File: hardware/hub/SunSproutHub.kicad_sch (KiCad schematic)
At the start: 48 parts, among them CN5 1755736, J4 BATTERY, J6 Qwiic Sys, J7 GPIO_HEADER_L, J8 GPIO_HEADER_R, Q1 MDD3415, Q2 DMP3098L-7, SW1 RESET, SW2 BOOT, U1 ESP32-C5-WROOM-1U

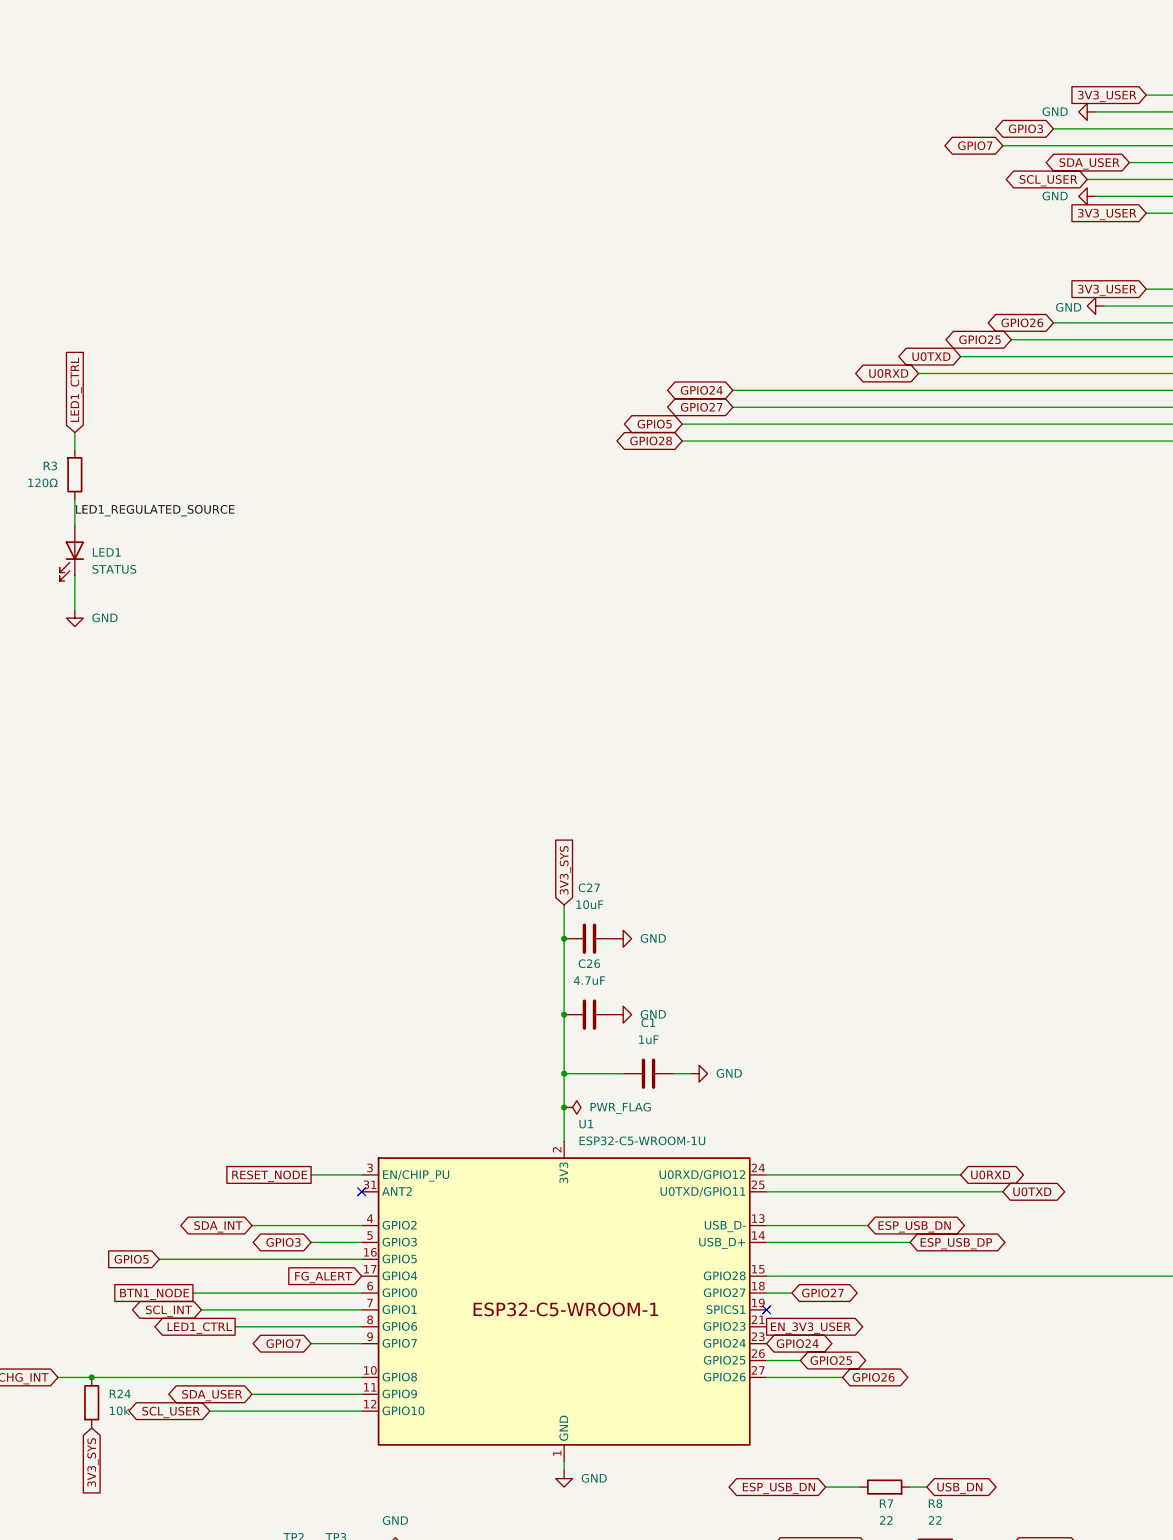
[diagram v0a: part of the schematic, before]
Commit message: Move the internal I2C clock to GPIO3 so both buses can run at once
The ESP32-C5 has one general-purpose I2C controller and one low-power
controller (datasheet 4.2.1.3: "ESP32-C5 has an I2C and an LP I2C bus
interface"). Running two I2C buses simultaneously needs both of them.

The general-purpose controller routes to any pin through the GPIO matrix. The
low-power one does not -- LP_I2C is wired through the LP IO MUX to GPIO2 for
data and GPIO3 for clock, and cannot be moved.

SDA_INT was already on GPIO2, but SCL_INT sat on GPIO1. That left neither bus
able to reach the low-power controller, so both contended for the single
general-purpose one and the firmware would not build. Caught while writing
example ESPHome firmware, before any board was fabricated.

SCL_INT now lands on GPIO3, which previously went only to the unfitted J7
expansion header. GPIO1 takes its place there as the spare, so no pin is lost.
The symbol pin names were updated to LP_I2C_SDA / LP_I2C_SCL to make the
constraint visible in the schematic.

This also gains something rather than just unblocking the build: LP peripherals
and the LP CPU stay powered in deep sleep, so the charger and fuel gauge on the
internal bus stay reachable while the main processor is off -- which suits a
node that sleeps ten minutes at a time.

Fixes a silkscreen mismatch found alongside it: J7 pin 3 read GPIO1 on the
front and GPIO3 on the back. All ten front/back label pairs now agree.

Verified with libraries present: DRC 0 violations, 0 unconnected, 0 schematic
parity; ERC matches the accepted baseline. Docs and board renders regenerated.

Co-Authored-By: Claude Opus 5 <noreply@anthropic.com>
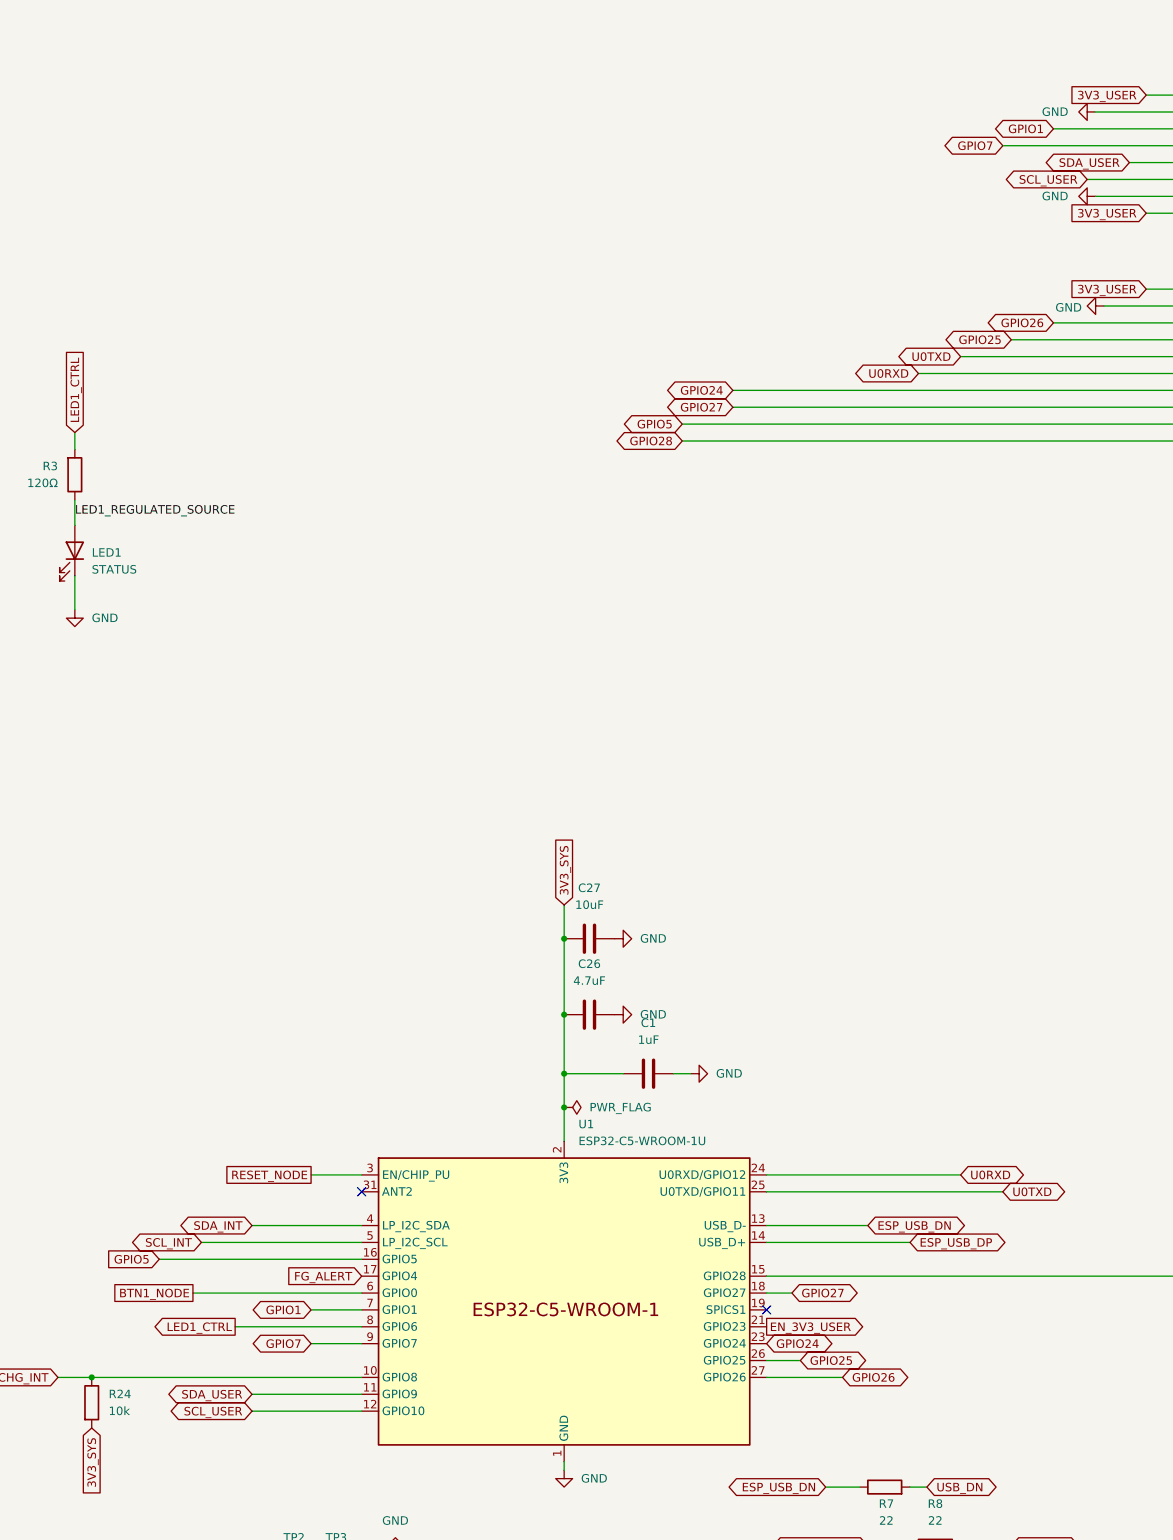
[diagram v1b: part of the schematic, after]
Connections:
- net SCL_INT: now also U1.5 (GPIO3); no longer U1.7 (GPIO1)
- net GPIO3 renamed GPIO1
- net GPIO1: now also U1.7 (GPIO1); no longer U1.5 (GPIO3)
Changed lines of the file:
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@@
 	(wire
 		(pts
+			(xy 405.13 227.33) (xy 381 227.33)
+		)
+		(stroke
+			(width 0)
+			(type default)
+		)
+	)
+	(wire
+		(pts
 			(xy 452.12 201.93) (xy 454.66 201.93)
 		)
@@
 	(wire
 		(pts
-			(xy 405.13 252.73) (xy 382.27 252.73)
+			(xy 405.13 252.73) (xy 388.62 252.73)
 		)
 		(stroke
@@
 	(wire
 		(pts
-			(xy 405.13 227.33) (xy 397.51 227.33)
-		)
-		(stroke
-			(width 0)
-			(type default)
-		)
-	)
-	(wire
-		(pts
 			(xy 474.98 264.16) (xy 480.06 264.16)
 		)
@@
 	(wire
 		(pts
-			(xy 405.13 237.49) (xy 381 237.49)
+			(xy 271.78 125.73) (xy 256.54 125.73)
 		)
 		(stroke
@@
 	(wire
 		(pts
-			(xy 271.78 125.73) (xy 256.54 125.73)
+			(xy 196.85 49.53) (xy 196.85 43.18)
 		)
 		(stroke
@@
 	(wire
 		(pts
-			(xy 196.85 49.53) (xy 196.85 43.18)
+			(xy 199.39 40.64) (xy 208.28 40.64)
 		)
 		(stroke
@@
 	(wire
 		(pts
-			(xy 199.39 40.64) (xy 208.28 40.64)
+			(xy 466.09 227.33) (xy 487.68 227.33)
 		)
 		(stroke
@@
 	(wire
 		(pts
-			(xy 466.09 227.33) (xy 487.68 227.33)
+			(xy 54.61 54.61) (xy 64.77 54.61)
 		)
 		(stroke
@@
 	(wire
 		(pts
-			(xy 54.61 54.61) (xy 64.77 54.61)
+			(xy 138.43 40.64) (xy 146.05 40.64)
 		)
 		(stroke
@@
 	(wire
 		(pts
-			(xy 138.43 40.64) (xy 146.05 40.64)
+			(xy 49.53 24.13) (xy 57.15 24.13)
 		)
 		(stroke
@@
 	(wire
 		(pts
-			(xy 49.53 24.13) (xy 57.15 24.13)
+			(xy 405.13 237.49) (xy 397.51 237.49)
 		)
 		(stroke
@@
 		)
 	)
-	(global_label "GPIO3"
+	(global_label "GPIO1"
 		(shape bidirectional)
 		(at 509.27 59.69 180)
@@
 		)
 	)
-	(global_label "SCL_INT"
-		(shape bidirectional)
-		(at 381 237.49 180)
-		(fields_autoplaced yes)
-		(effects
-			(font
-				(size 1.27 1.27)
-			)
-			(justify right)
-		)
-		(property "Intersheetrefs" "${INTERSHEET_REFS}"
-			(at 369.5254 237.49 0)
-			(hide yes)
-			(show_name no)
-			(do_not_autoplace no)
-			(effects
-				(font
-					(size 1.27 1.27)
-				)
-				(justify right)
-			)
-		)
-	)
 	(global_label "USB_DATA_RAW_P"
 		(shape output)
@@
 		)
 	)
+	(global_label "SCL_INT"
+		(shape bidirectional)
+		(at 381 227.33 180)
+		(fields_autoplaced yes)
+		(effects
+			(font
+				(size 1.27 1.27)
+			)
+			(justify right)
+		)
+		(property "Intersheetrefs" "${INTERSHEET_REFS}"
+			(at 369.5254 227.33 0)
+			(hide yes)
+			(show_name no)
+			(do_not_autoplace no)
+			(effects
+				(font
+					(size 1.27 1.27)
+				)
+				(justify right)
+			)
+		)
+	)
 	(global_label "GPIO24"
 		(shape bidirectional)
@@
 		)
 	)
+	(global_label "GPIO1"
+		(shape bidirectional)
+		(at 397.51 237.49 180)
+		(fields_autoplaced yes)
+		(effects
+			(font
+				(size 1.27 1.27)
+			)
+			(justify right)
+		)
+		(property "Intersheetrefs" "${INTERSHEET_REFS}"
+			(at 387.7287 237.49 0)
+			(hide yes)
+			(show_name no)
+			(do_not_autoplace no)
+			(effects
+				(font
+					(size 1.27 1.27)
+				)
+				(justify right)
+			)
+		)
+	)
 	(global_label "SCL_USER"
 		(shape bidirectional)
-		(at 382.27 252.73 180)
+		(at 388.62 252.73 180)
 		(fields_autoplaced yes)
 		(effects
@@
 		)
 		(property "Intersheetrefs" "${INTERSHEET_REFS}"
-			(at 368.7393 252.73 0)
+			(at 375.0893 252.73 0)
 			(hide yes)
 			(show_name no)
@@
 		)
 	)
-	(global_label "GPIO3"
-		(shape bidirectional)
-		(at 397.51 227.33 180)
-		(fields_autoplaced yes)
-		(effects
-			(font
-				(size 1.27 1.27)
-			)
-			(justify right)
-		)
-		(property "Intersheetrefs" "${INTERSHEET_REFS}"
-			(at 387.7287 227.33 0)
-			(hide yes)
-			(show_name no)
-			(do_not_autoplace no)
-			(effects
-				(font
-					(size 1.27 1.27)
-				)
-				(justify right)
-			)
-		)
-	)
 	(global_label "U0RXD"
 		(shape bidirectional)
@@
 		)
 		(pin "4"
+			(alternate "LP_I2C_SDA")
 		)
 		(pin "5"
+			(alternate "LP_I2C_SCL")
 		)
 		(pin "6"
@@
 			"169d7c5d-38f7-4ee4-bc29-ffcfbb4e3a81" "1e1dbc50-1092-427c-8870-8d631a060adb"
 			"1e242c7c-7119-4160-b32e-ce540edb2e90" "20197bd1-f55d-4f2a-ad00-546ee6796090"
-			"2343f6f0-71fb-471e-acb5-091c9866b876" "2440bf78-0345-4839-84a7-00de48950a9a"
-			"2a86e73b-fc8d-4b98-9e81-52da14f3f9e2" "2c452db6-6001-4afa-9e44-e907b449f8be"
-			"33f36117-02b8-4e79-9091-6ba55d1b04f2" "36690580-b943-4629-9957-aa396383c732"
-			"3717ba9a-354d-420e-9c9a-7e86c9107e4e" "37736c54-73b5-48ea-b0d4-a23ee8a6ab56"
+			"2440bf78-0345-4839-84a7-00de48950a9a" "2a86e73b-fc8d-4b98-9e81-52da14f3f9e2"
+			"2c452db6-6001-4afa-9e44-e907b449f8be" "33f36117-02b8-4e79-9091-6ba55d1b04f2"
+			"36690580-b943-4629-9957-aa396383c732" "3717ba9a-354d-420e-9c9a-7e86c9107e4e"
+			"37736c54-73b5-48ea-b0d4-a23ee8a6ab56" "37fd69d6-3873-4793-ac15-176e5f41edae"
 			"3882554a-a669-409c-b109-d2db0f0de7b7" "3bc05008-9849-4492-a9e8-462eb1134877"
 			"3c010637-2eb0-4284-a55c-d06e1dd6bd9e" "3e065a1b-e98f-4dd1-90e0-d47686c678b3"
@@
 			"5d24c831-cbd8-4c16-badc-b212c181ec05" "602462ac-073d-4cea-8ca9-cace28e6233b"
 			"66782692-f0bb-4117-99b7-8cdfa24af31b" "68feab76-7c33-42d7-8d89-1607d456debc"
-			"69fb908a-66a5-4a21-8b4d-d596f0dbfb3a" "7137d51a-70a5-4bb2-b5d8-4879c003a661"
-			"727ed8ac-55ee-4f1c-bfee-10c0dff09eb9" "73393bb5-6cbc-4c09-8557-df134a663986"
+			"69fb908a-66a5-4a21-8b4d-d596f0dbfb3a" "6e211dc5-9696-48ec-a86d-d5c3db20e372"
+			"7137d51a-70a5-4bb2-b5d8-4879c003a661" "73393bb5-6cbc-4c09-8557-df134a663986"
 			"73b7e93b-41f2-4ad7-9804-f49adc7998f6" "757df0c4-b2a4-4e9c-bcdf-46db3bbec0e3"
 			"777be74b-050d-4c2b-9571-055d8ddebad4" "7a7383f7-9beb-4228-881b-e845f730bf84"
@@
 			"85395603-badd-45eb-8570-5a8c34dba823" "884d2110-7b83-4aa6-bf99-8ffea8940d96"
 			"8b361dec-e5b8-45ee-a57d-0a416130dc36" "8d1f2a89-aeaf-401e-8b4d-fc1c6bad8559"
-			"8dc6bc6a-ddf3-4671-be20-c125de1509c4" "8edee379-ad4f-41ea-bfca-e68e3c407b1c"
-			"969a7123-78b7-4123-9ab8-a0bf88c1aef8" "96f21437-5df5-45a6-8e68-ec7e1cf11af5"
-			"97b26be0-90cc-45e7-a6f5-af9f984319c6" "98533b4e-f7a0-4a97-ab9e-dd6a35b22f03"
+			"8dc6bc6a-ddf3-4671-be20-c125de1509c4" "969a7123-78b7-4123-9ab8-a0bf88c1aef8"
+			"96f21437-5df5-45a6-8e68-ec7e1cf11af5" "97b26be0-90cc-45e7-a6f5-af9f984319c6"
+			"98533b4e-f7a0-4a97-ab9e-dd6a35b22f03" "9d4d6477-5097-40da-ae23-4d3bfeee29e6"
 			"9e179791-0768-4ee8-bbf2-b55000177ddf" "a0e2762e-5aed-4efb-a840-4499248989a7"
 			"a1e06de7-0d00-4e92-b0e1-9f9ad78e0c84" "a23e7e29-4868-4492-a266-94c4c90bca87"
@@
 			"ab2c0d26-6318-4e84-b091-cd369ba6adcb" "b0c0a721-5dfc-4c91-a1da-83c8d9d61a98"
 			"b43f4762-4b8b-4a0c-8473-ed0c95bccb0a" "b53dedbc-8629-4367-82dd-91e5ce1418c6"
-			"b55d6f8c-f03b-4c33-8bc7-43e6833ccc6c" "bb79576f-d908-4dc5-b33c-8d6f337736d1"
-			"bba8b4ce-27ec-4a70-b19c-22b303f6f61f" "bdf77e5c-c45b-4d77-ae2d-326907510e99"
-			"c02b3493-f5d4-4f01-b2b0-5fec90cbf0f8" "c4cce21b-c9f5-4595-a354-c56622915032"
-			"c4f6556c-30e7-4da8-b7e0-240d66649dc1" "c55e46da-e0d5-4969-aace-60dc2423665f"
-			"c99124ac-9dbc-4d49-abbb-d4c945b7798b" "ce702160-66a7-4176-a4bc-d64b35d29057"
-			"d298a078-c36e-4431-94f6-cd4cbbc04737" "d3a6a647-7e46-4873-a382-bf0a1f1e989b"
+			"b55d6f8c-f03b-4c33-8bc7-43e6833ccc6c" "baf1f15e-455b-46e6-b24c-ef7d0017e682"
+			"bb79576f-d908-4dc5-b33c-8d6f337736d1" "bba8b4ce-27ec-4a70-b19c-22b303f6f61f"
+			"bdf77e5c-c45b-4d77-ae2d-326907510e99" "c02b3493-f5d4-4f01-b2b0-5fec90cbf0f8"
+			"c4cce21b-c9f5-4595-a354-c56622915032" "c4f6556c-30e7-4da8-b7e0-240d66649dc1"
+			"c55e46da-e0d5-4969-aace-60dc2423665f" "c99124ac-9dbc-4d49-abbb-d4c945b7798b"
+			"ce702160-66a7-4176-a4bc-d64b35d29057" "d298a078-c36e-4431-94f6-cd4cbbc04737"
 			"d48ffa0d-670a-4652-9cc6-267fa3b779f2" "d6b72293-1d2a-4f4d-af34-cde4e34292f6"
 			"da70442b-516c-41f5-8f3f-01d4d4aa00e2" "dfad61fe-f939-487a-8328-ba2296c3723c"

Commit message: Clamp Q2's gate so the DC input can run to the charger's full 24 V (#1)
* Clamp Q2's gate so the DC input can run to the charger's full 24 V

The solar/DC reverse-polarity FET Q2 is self-biased: its gate sits at ground
through R19, so the full input voltage appears across the gate oxide. That is
true in normal operation, not only under a reversed source - a correctly
connected 24 V panel stresses the gate exactly as hard as a backwards one. The
DMP3098L-7's +/-20 V gate rating therefore capped the usable input at 20 V,
below the 24 V the BQ25798 itself accepts. The protection, not the charger, was
setting the ceiling.

D2 (BZT52C12S, 12 V zener, LCSC C19077447) clamps gate-to-source: cathode to
the source at CN5 pin 1, anode to the gate. Above roughly 12 V in it holds Vgs
near -12 V; reversed, it holds it near +0.7 V. R19 stays at 100 kOhm, giving
120 uA of clamp current at 24 V in - deliberately below the zener's 5 mA test
current, since reaching the knee would need R19 near 2.4 kOhm and draw 5 mA
continuously from the panel.

Also carries the PCB v2 IC and passive validation work: the ship-FET addition,
the PWR_FLAGs that resolve the power_pin_not_driven ERC entries, and the
charger, fuel-gauge, regulator and I2C-buffer sheet updates documented
alongside them.

Tooling, alongside the design change:

  - tools/run_kicad_validation.sh called tools/validation/check_violations.py
    with known_exceptions.json. Neither file has ever been committed, so the
    local pre-flight failed on every run since the initial commit. It now calls
    tools/check_erc_baseline.py against erc-baseline.json, mirroring
    .github/workflows/validate-hardware.yml - errors only, and DRC gains
    --refill-zones and --exit-code-violations. CI was never affected.
  - The ERC baseline is now empty. All five accepted entries were
    power_pin_not_driven, and the PWR_FLAGs resolve every one. An empty
    baseline is stricter: nothing is absorbed by a matching entry any more.
  - Ignore hardw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
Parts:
- added D2: BZT52C12S, PCM_JLCPCB:D_SOD-323, symbol PCM_JLCPCB-Diodes:Zener,BZT52C12S
- added Q3: AO3400A, Snapeda:SOT95P280X125-3N, symbol Snapeda:AO3400A
- added TP15: VBAT_PRO, PCM_SparkFun-Connector:TestPoint-1.0mm, symbol PCM_SparkFun-Connector:TestPoint_1.0mm
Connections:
- net VBAT: now also Q3.2; no longer Q1.3 (D)
- net at CN5.1, Q2.2 (S): now also D2.1
- net VBAT_RAW: now reaches J4.1 (Pin_1), Q1.2 (S)
- net at Q2.1 (G), R19.1: now also D2.2
- new net SDRV_NODE: Q3.1
- new net VBAT_PROTECTED: Q1.3 (D), Q3.3, TP15.1
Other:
- moved on the sheet: J4, NT4, Q1, R17, R19, R60, TP14
